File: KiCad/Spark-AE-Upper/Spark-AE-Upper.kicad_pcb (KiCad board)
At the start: 2 copper layers, 50 x 100 mm, 21 parts, among them J1 SSM-120-L-SV-BE, J2 SSM-120-L-SV-BE, J3 Conn_02x05_Odd_Even, J4 Conn_02x05_Odd_Even, J5 Conn_01x08_Socket, J6 Conn_01x08_Socket, J7 USB_C_Receptacle, SW1 SW_Push, SW2 SW_Push, U1 PJS008U-3000-0

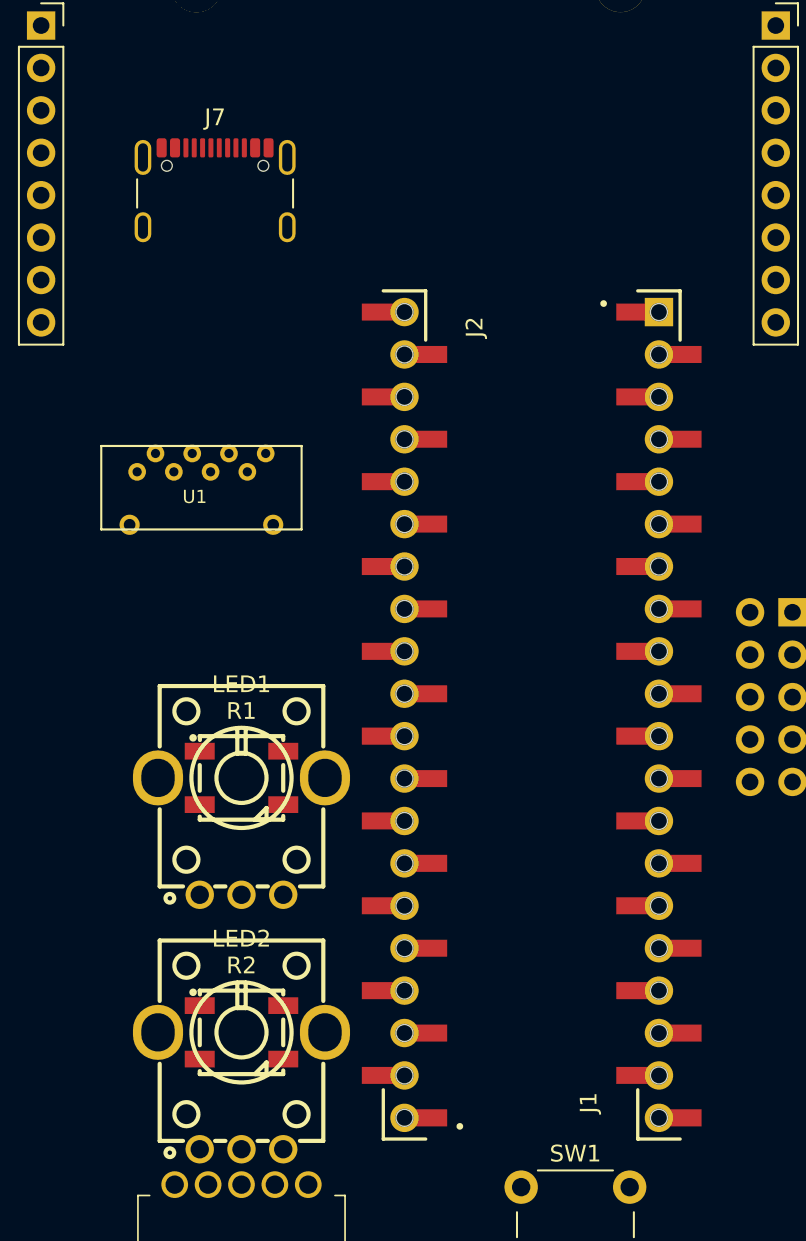
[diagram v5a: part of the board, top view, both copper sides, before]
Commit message: repositioned daisy seed, usb c, and micro sd
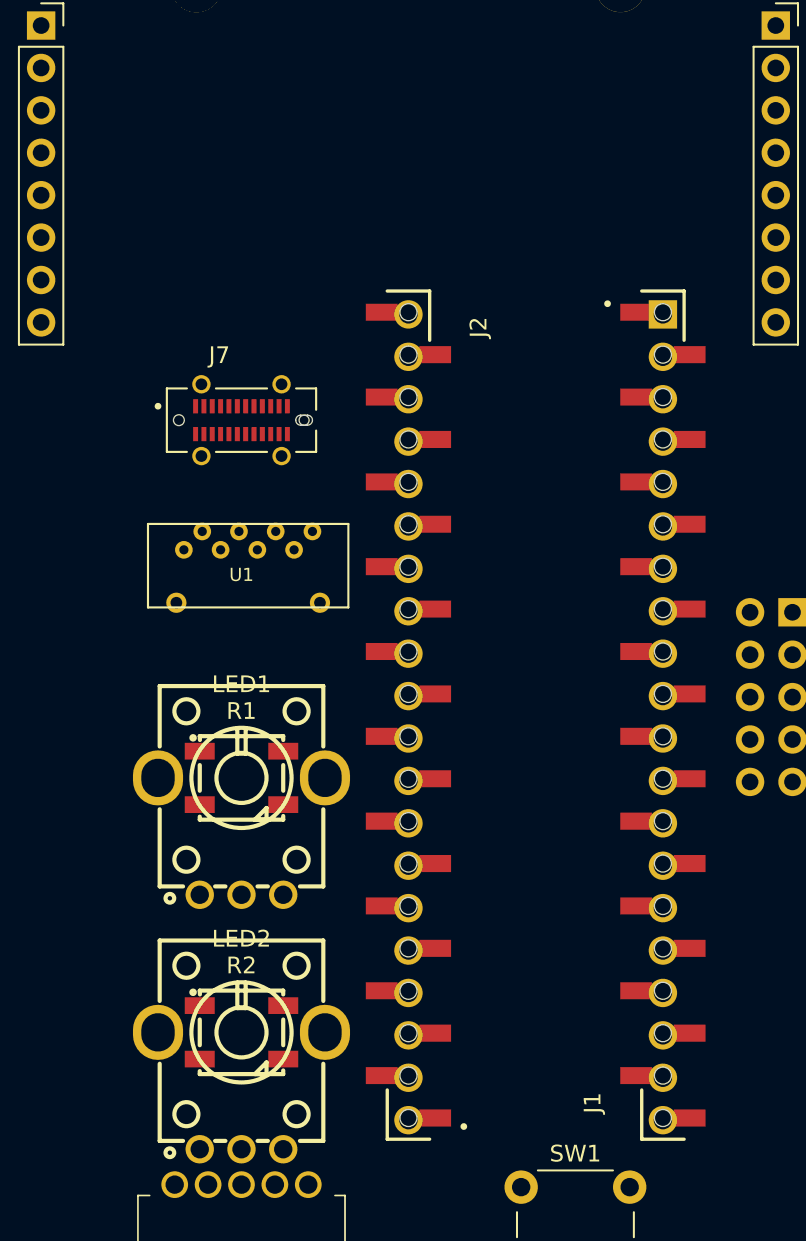
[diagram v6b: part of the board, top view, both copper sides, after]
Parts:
- removed A1: Electrosmith_Daisy_Seed_Rev4, clectric-diy:DAISY_SEED
- added U2: Daisy_Seed, clectric-diy:DAISY_SEED, B.Cu at (135.8, 71.0)
- J7: value USB_C_Receptacle -> UJ32-C-V-G-TH-5-P24-TR; footprint Connector_USB:USB_C_Receptacle_GCT_USB4105-xx-A_16P_TopMnt_Horizontal -> clectric-diy:SAMESKY_UJ32-C-V-G-TH-5-P24-TR
- moved J7 12.7 mm to (110.6, 77.4)
- moved U1 5.45 mm to (110.6, 86.6)
- moved J1 0.24 mm to (135.8, 95.0)
- moved J2 0.24 mm to (120.6, 95.0)
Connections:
- J4 pad 1: unconnected-(J4-Pin_1-Pad1) -> 5V
- J4 pad 10: unconnected-(J4-Pin_10-Pad10) -> CLOCK
- J4 pad 2: unconnected-(J4-Pin_2-Pad2) -> 5V
- J4 pad 3: unconnected-(J4-Pin_3-Pad3) -> GND
- J4 pad 4: unconnected-(J4-Pin_4-Pad4) -> GND
- J4 pad 5: unconnected-(J4-Pin_5-Pad5) -> CV
- J4 pad 6: unconnected-(J4-Pin_6-Pad6) -> GATE
- J4 pad 7: unconnected-(J4-Pin_7-Pad7) -> START
- J4 pad 8: unconnected-(J4-Pin_8-Pad8) -> STOP
- J4 pad 9: unconnected-(J4-Pin_9-Pad9) -> CTRL
- J5 pad 1: unconnected-(J5-Pin_1-Pad1) -> AUDIO_IN_1
- J5 pad 2: unconnected-(J5-Pin_2-Pad2) -> AUDIO_IN_2
- J6 pad 1: unconnected-(J6-Pin_1-Pad1) -> AUDIO_OUT_1
- J6 pad 2: unconnected-(J6-Pin_2-Pad2) -> AUDIO_OUT_2
- J7 pad A1: Net-(J7-GND-PadA1) -> unconnected-(J7-GND-PadA1)
- J7 pad A12: Net-(J7-GND-PadA1) -> unconnected-(J7-GND__1-PadA12)
- J7 pad A4: Net-(J7-VBUS-PadA4) -> unconnected-(J7-VBUS-PadA4)
- J7 pad A9: Net-(J7-VBUS-PadA4) -> unconnected-(J7-VBUS__1-PadA9)
- J7 pad B1: Net-(J7-GND-PadA1) -> unconnected-(J7-GND__2-PadB1)
- J7 pad B12: Net-(J7-GND-PadA1) -> unconnected-(J7-GND__3-PadB12)
- J7 pad B4: Net-(J7-VBUS-PadA4) -> unconnected-(J7-VBUS__2-PadB4)
- J7 pad B9: Net-(J7-VBUS-PadA4) -> unconnected-(J7-VBUS__3-PadB9)

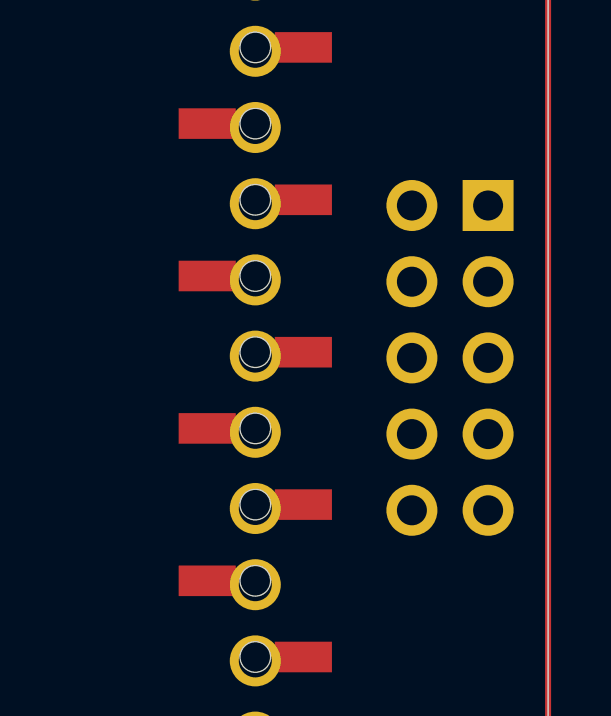
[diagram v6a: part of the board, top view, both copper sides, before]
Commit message: added nets for ae modular i/o headers
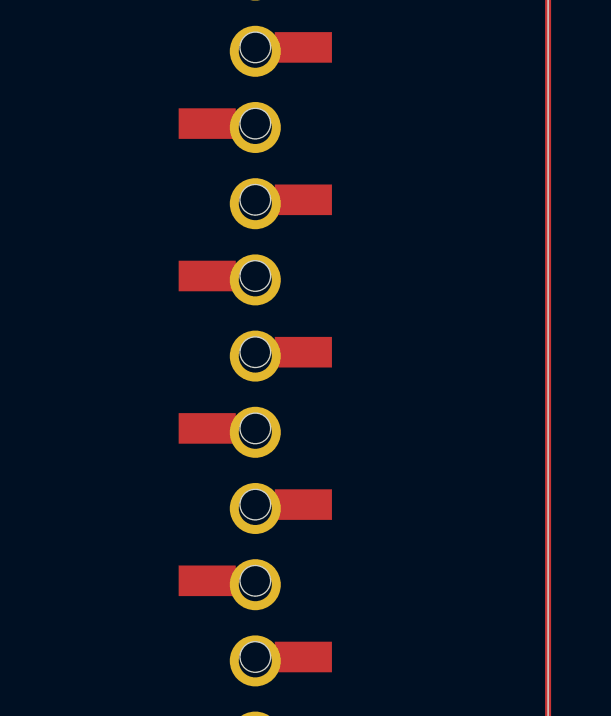
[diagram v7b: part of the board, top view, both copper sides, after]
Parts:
- removed J3: Conn_02x05_Odd_Even, Connector_PinHeader_2.54mm:PinHeader_2x05_P2.54mm_Vertical
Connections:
- LED1 pad 1: Net-(LED1-DIN) -> unconnected-(LED1-VDD-Pad1)
- LED1 pad 3: Net-(LED1-DIN) -> unconnected-(LED1-DIN-Pad3)

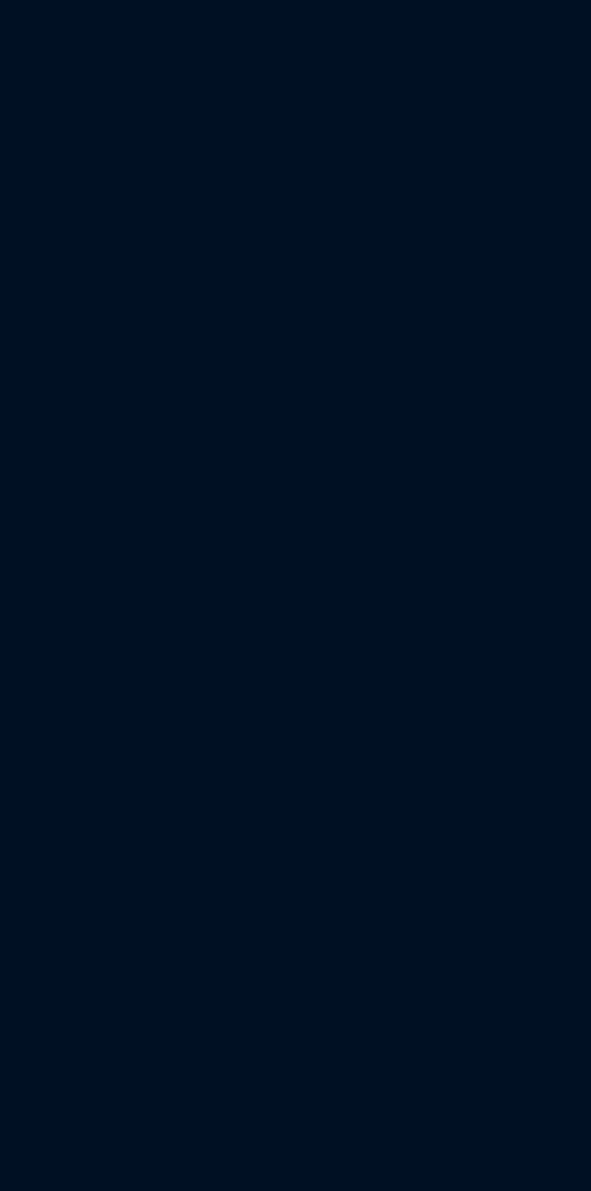
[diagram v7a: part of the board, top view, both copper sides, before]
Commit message: renamed nets to match pod and added arc connector
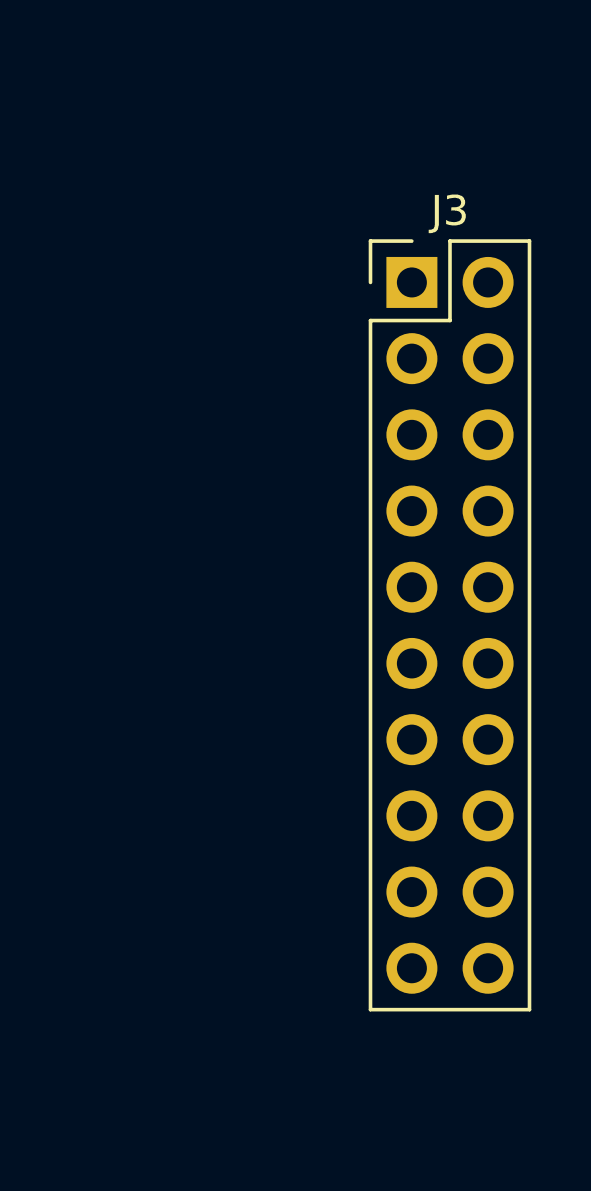
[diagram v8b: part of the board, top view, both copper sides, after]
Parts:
- added J3: Conn_02x10_Odd_Even, Connector_PinHeader_2.54mm:PinHeader_2x10_P2.54mm_Vertical, F.Cu at (166.5, 75.2)
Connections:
- net 3V3_A renamed +3V3_A
- net 3V3_D renamed +3V3_D
- net 5V renamed +5V
- net A0_D15 renamed POT_2
- net A10_D25 renamed ENC_B
- net A11_D28 renamed TAC_SWITCH_2
- net A2_D17 renamed LED_2_R
- net A3_D18 renamed LED_1_B
- net A4_D19 renamed LED_1_G
- net A5_D20 renamed LED_1_R
- net A6_D21 renamed POT_1
- net A8_D23 renamed LED_2_B
- net A9_D24 renamed LED_2_G
- net D0 renamed USB_OTG_FS_ID
- net D1 renamed SD_D3
- net D10 renamed SPI_MOSI
- net D11 renamed I2C_SCL
- net D12 renamed I2C_SDA
- net D13 renamed ENC_CLICK
- net D14 renamed USART1_RX
- net D2 renamed SD_D2
- net D26 renamed ENC_A
- net D27 renamed TAC_SWITCH_1
- net D29 renamed USB_OTG_FS_D-
- net D3 renamed SD_D1
- net D30 renamed USB_OTG_FS_D+
- net D4 renamed SD_D0
- net D5 renamed SD_CMD
- net D6 renamed SD_CK
- net D7 renamed SPI_NSS
- net D8 renamed SPI_SCK
- net D9 renamed SPI_MISO
- J1 pad 20: AGND -> GND
- J2 pad 20: DGND -> GND
- J4 pad 10: CLOCK -> STOP
- J4 pad 8: STOP -> CLOCK
- U2 pad 20: AGND -> GND
- U2 pad 40: DGND -> GND
